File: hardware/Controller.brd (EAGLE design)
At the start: 38.1 x 58.4 mm, 69 parts, among them Q1 MOSFET-NCHANNEL2N7002PW, Q2 BSS84PW, Q3 BSS84PW, U3 MMA8652FC, U4 MCP6002MS, U5 TXS0101DCK, U6 LCD_1.8, U7 VREG

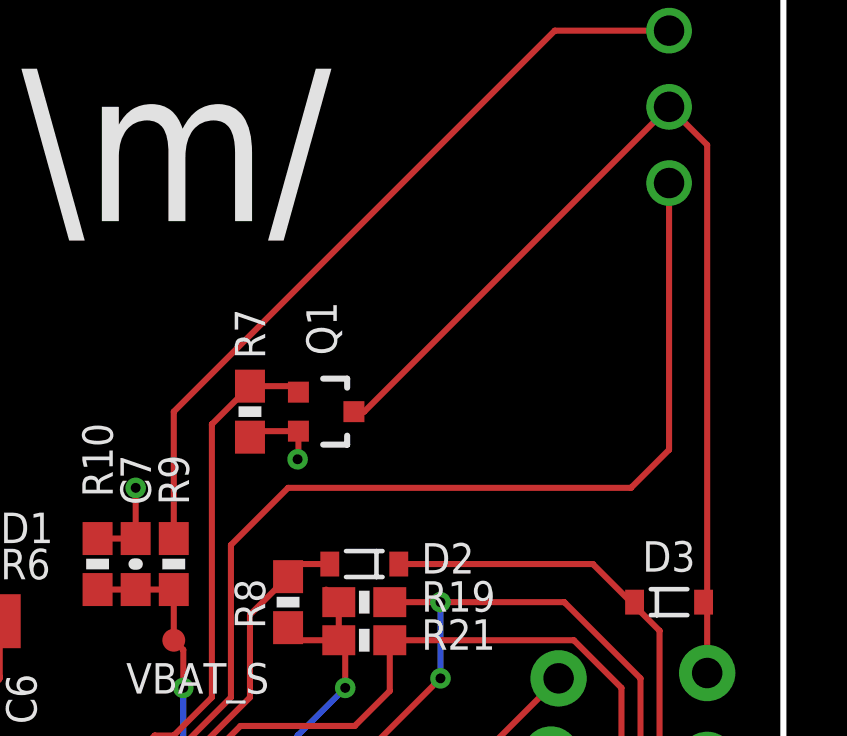
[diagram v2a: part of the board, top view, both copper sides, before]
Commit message: hardware: divide PGOOD to be 3.3V
It is a 5V signal, previously fed into a non-5V tolerant pin.
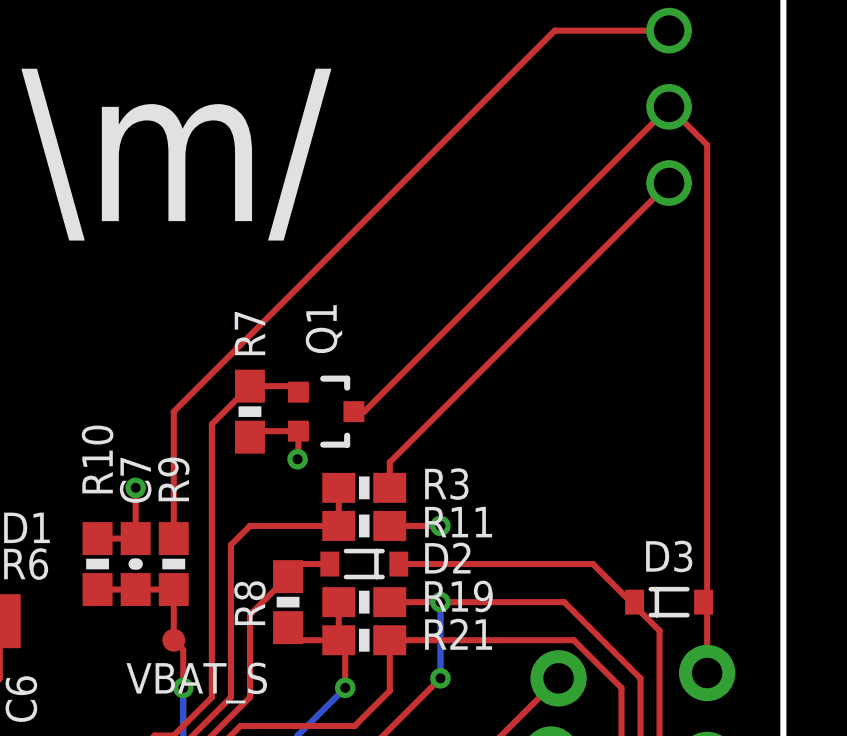
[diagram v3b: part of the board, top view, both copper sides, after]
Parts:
- added R11: 150k, SparkFun-Resistors:0603-RES
- added R3: 100k, SparkFun-Resistors:0603-RES
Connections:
- new net N$8: R3.2, U7.PGOOD
- net GND: now also R11.1
- net PGOOD: now also R11.2, R3.1; no longer U7.PGOOD
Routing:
- net PGOOD: track 35.8 -> 16.2 mm
- net N$8: track 0.00 -> 14.0 mm
- net GND: track 30.7 -> 33.0 mm, vias 10 -> 11
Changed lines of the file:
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@@
 <layer number="23" name="tOrigins" color="15" fill="1" visible="yes" active="yes"/>
 <layer number="24" name="bOrigins" color="15" fill="1" visible="yes" active="yes"/>
-<layer number="25" name="tNames" color="7" fill="1" visible="no" active="yes"/>
-<layer number="26" name="bNames" color="7" fill="1" visible="no" active="yes"/>
+<layer number="25" name="tNames" color="7" fill="1" visible="yes" active="yes"/>
+<layer number="26" name="bNames" color="7" fill="1" visible="yes" active="yes"/>
 <layer number="27" name="tValues" color="7" fill="1" visible="no" active="yes"/>
 <layer number="28" name="bValues" color="7" fill="1" visible="no" active="yes"/>
@@
 <layer number="50" name="dxf" color="7" fill="1" visible="no" active="no"/>
 <layer number="51" name="tDocu" color="6" fill="1" visible="yes" active="yes"/>
-<layer number="52" name="bDocu" color="7" fill="1" visible="no" active="yes"/>
+<layer number="52" name="bDocu" color="7" fill="1" visible="yes" active="yes"/>
 <layer number="53" name="tGND_GNDA" color="7" fill="9" visible="no" active="no"/>
 <layer number="54" name="bGND_GNDA" color="1" fill="9" visible="no" active="no"/>
@@
 <attribute name="VALUE" x="35.306" y="7.493" size="0.4064" layer="27" font="vector" rot="R180"/>
 </element>
+<element name="R3" library="SparkFun-Resistors" package="0603-RES" value="100k" x="24.13" y="36.83" smashed="yes">
+<attribute name="NAME" x="26.035" y="36.449" size="1.016" layer="25" ratio="14"/>
+<attribute name="VALUE" x="23.114" y="35.687" size="0.4064" layer="27" font="vector"/>
+</element>
+<element name="R11" library="SparkFun-Resistors" package="0603-RES" value="150k" x="24.13" y="35.56" smashed="yes" rot="R180">
+<attribute name="NAME" x="26.035" y="35.179" size="1.016" layer="25" ratio="14"/>
+<attribute name="VALUE" x="25.146" y="36.703" size="0.4064" layer="27" font="vector" rot="R180"/>
+</element>
 </elements>
 <signals>
@@
 <wire x1="2.96" y1="17.565" x2="3.175" y2="17.78" width="0.2032" layer="1"/>
 <via x="3.175" y="17.78" extent="1-16" drill="0.3302"/>
+<contactref element="R11" pad="1"/>
+<wire x1="24.98" y1="35.56" x2="25.4" y2="35.14" width="0.2032" layer="1"/>
+<via x="26.67" y="35.56" extent="1-16" drill="0.3302"/>
+<wire x1="26.67" y1="35.56" x2="24.98" y2="35.56" width="0.2032" layer="1"/>
 <wire x1="30.607" y1="25.4" x2="29.210240625" y2="15.519534375" width="0" layer="19" extent="16-16"/>
 </signal>
@@
 </signal>
 <signal name="PGOOD">
-<contactref element="U7" pad="PGOOD"/>
 <contactref element="U1" pad="7"/>
 <wire x1="15.83" y1="25.86" x2="15.83" y2="26.625" width="0.2032" layer="1"/>
@@
 <wire x1="17.78" y1="27.94" x2="19.685" y2="29.845" width="0.2032" layer="1"/>
 <wire x1="19.685" y1="29.845" x2="19.685" y2="34.925" width="0.2032" layer="1"/>
-<wire x1="19.685" y1="34.925" x2="21.59" y2="36.83" width="0.2032" layer="1"/>
-<wire x1="21.59" y1="36.83" x2="33.02" y2="36.83" width="0.2032" layer="1"/>
-<wire x1="33.02" y1="36.83" x2="34.29" y2="38.1" width="0.2032" layer="1"/>
-<wire x1="34.29" y1="38.1" x2="34.29" y2="46.99" width="0.2032" layer="1"/>
+<contactref element="R3" pad="1"/>
+<contactref element="R11" pad="2"/>
+<wire x1="23.28" y1="36.83" x2="23.28" y2="35.56" width="0.2032" layer="1"/>
+<wire x1="19.685" y1="34.925" x2="20.32" y2="35.56" width="0.2032" layer="1"/>
+<wire x1="20.32" y1="35.56" x2="23.28" y2="35.56" width="0.2032" layer="1"/>
 </signal>
 <signal name="VBAT_SENSE">
@@
 <wire x1="24.13" y1="7.895" x2="24.13" y2="9.31" width="0.4064" layer="1"/>
 </signal>
+<signal name="N$8">
+<contactref element="U7" pad="PGOOD"/>
+<contactref element="R3" pad="2"/>
+<wire x1="34.29" y1="46.99" x2="24.98" y2="37.68" width="0.2032" layer="1"/>
+<wire x1="24.98" y1="37.68" x2="24.98" y2="36.83" width="0.2032" layer="1"/>
+</signal>
 </signals>
